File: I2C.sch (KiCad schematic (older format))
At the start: 13 parts

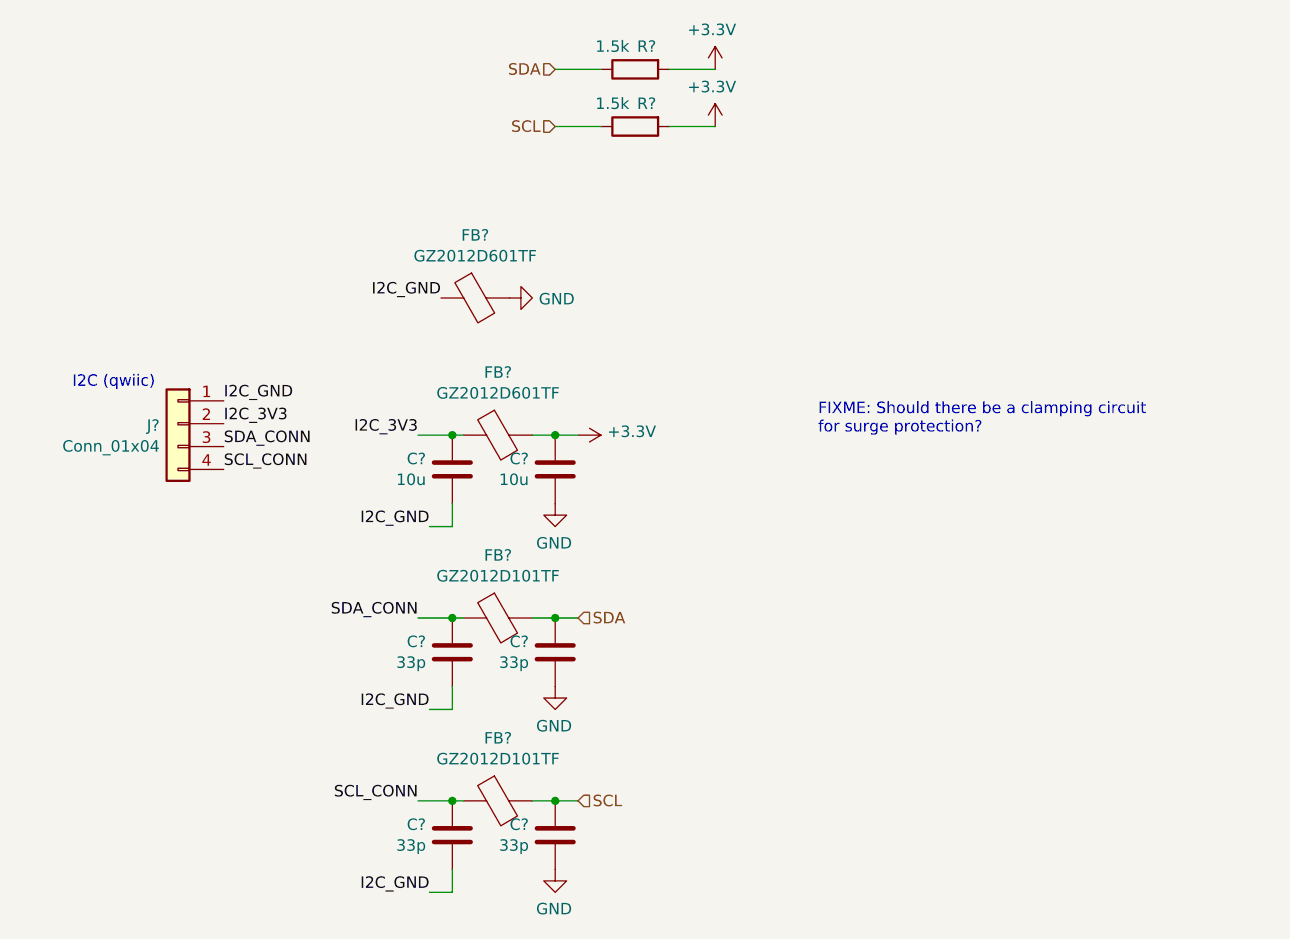
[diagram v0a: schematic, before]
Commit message: Update according to comments
Also add missing connectors and update the fuses
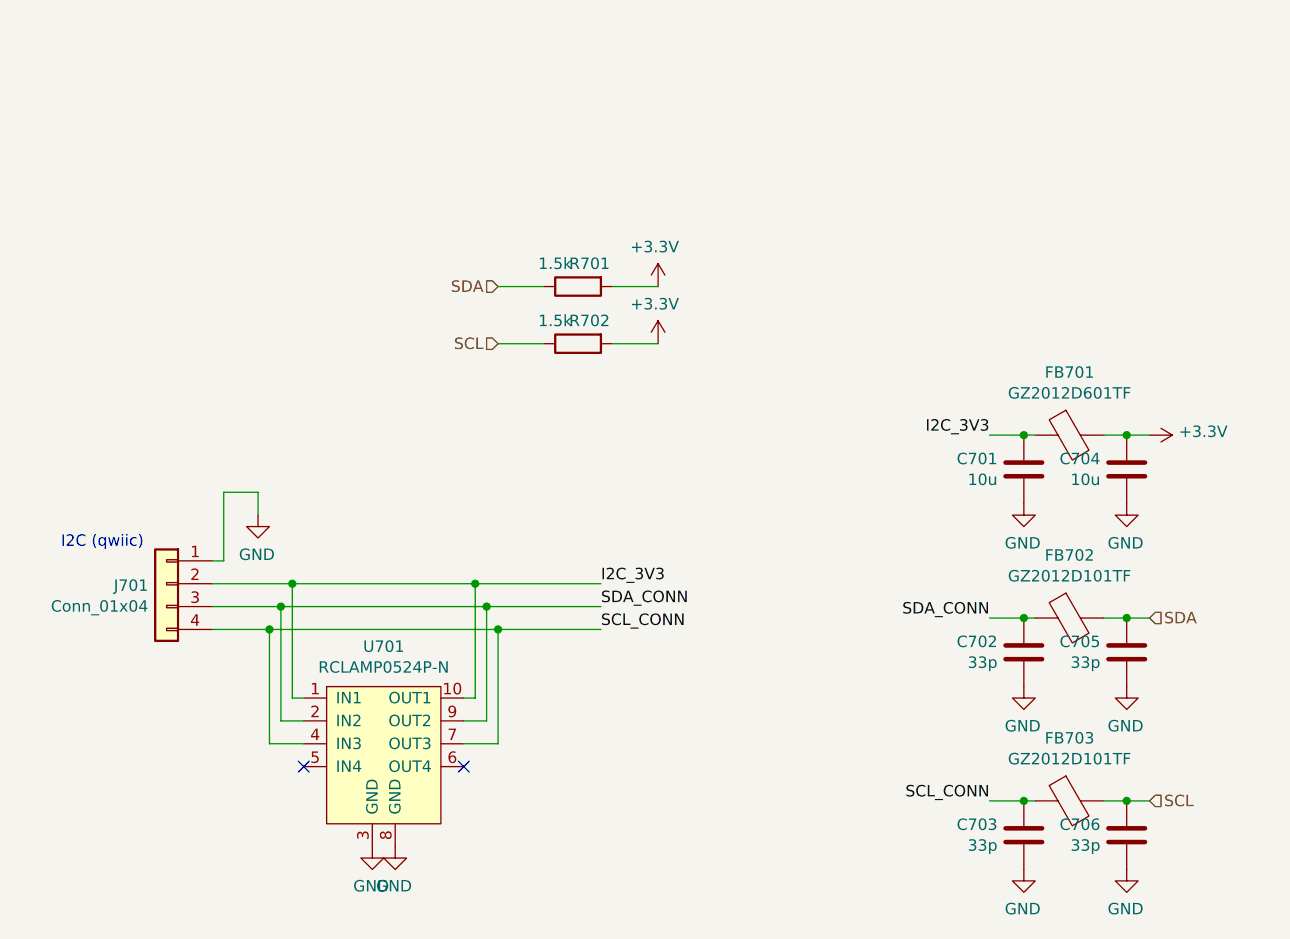
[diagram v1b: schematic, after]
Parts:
- removed FB?: GZ2012D601TF, symbol Device:Ferrite_Bead
- added U701: RCLAMP0524P-N, symbol SH-ESP32:RCLAMP0524P-N
- gave numbers to parts that had none: 12
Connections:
- net I2C_GND is gone; now on net GND: C701.2, C702.2, C703.2, J701.1 (Pin_1)
- net GND: now also U701.3 (GND), U701.8 (GND)
- net I2C_3V3: now also U701.1 (IN1), U701.10 (OUT1)
- net SCL_CONN: now also U701.4 (IN3), U701.7 (OUT3)
- net SDA_CONN: now also U701.2 (IN2), U701.9 (OUT2)
- no-connect marks 0 -> 2
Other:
- note removed: "FIXME: Should there be a clamping circuit\nfor surge protection?"
- moved on the sheet: C701, C702, C703, C704, C705, C706, FB701, FB702, FB703, J701, R701, R702

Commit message: Rough PCB layout
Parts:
- added J702: Conn_01x04, Connector_PinHeader_2.54mm:PinHeader_1x04_P2.54mm_Vertical, symbol Connector_Generic:Conn_01x04
- C701: value 10u -> 10uF; footprint (none) -> Capacitor_SMD:C_0402_1005Metric
- C702, C703: value 33p -> 33pF; footprint (none) -> Capacitor_SMD:C_0402_1005Metric
- C704: value 10u -> 10uF/50V; footprint (none) -> Capacitor_SMD:C_1206_3216Metric
- C705, C706: value 33p -> 33pF/50V; footprint (none) -> Capacitor_SMD:C_0603_1608Metric
- FB701, FB702, FB703: footprint (none) -> Inductor_SMD:L_0805_2012Metric
- J701: footprint (none) -> Connector_JST:JST_SH_BM04B-SRSS-TB_1x04-1MP_P1.00mm_Vertical
- R701, R702: footprint (none) -> Resistor_SMD:R_0402_1005Metric
- U701: footprint (none) -> Package_DFN_QFN:Diodes_UDFN-10_1.0x2.5mm_P0.5mm
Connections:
- net +3V3: now also C701.1; no longer C704.1
- net GND: now also J702.1 (Pin_1)
- net I2C_3V3: now also C704.1, J702.2 (Pin_2); no longer C701.1
- net SCL: now also C703.1; no longer C706.1
- net SCL_CONN: now also C706.1, J702.4 (Pin_4); no longer C703.1
- net SDA: now also C702.1; no longer C705.1
- net SDA_CONN: now also C705.1, J702.3 (Pin_3); no longer C702.1
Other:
- moved on the sheet: C701, C702, C703, C704, C705, C706

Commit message: Specified JLCPCB footprints for components
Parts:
- C701: LCSC (none) -> C15525
- C702, C703: LCSC (none) -> C1562
- C704: LCSC (none) -> C13585
- C705, C706: LCSC (none) -> C1663
- FB701: LCSC (none) -> C1017
- FB702, FB703: LCSC (none) -> C1015
- J701: LCSC (none) -> C145961
- J702: LCSC (none) -> C358686
- R701, R702: LCSC (none) -> C25867
- U701: LCSC (none) -> C316044
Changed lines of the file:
@@
 F 2 "Connector_JST:JST_SH_BM04B-SRSS-TB_1x04-1MP_P1.00mm_Vertical" H 1650 3350 50  0001 C CNN
 F 3 "~" H 1650 3350 50  0001 C CNN
+F 4 "C145961" H 1650 3350 50  0001 C CNN "LCSC"
 	1    1650 3350
 	-1   0    0    -1
@@
 F 2 "Capacitor_SMD:C_0603_1608Metric" H 5438 4300 50  0001 C CNN
 F 3 "~" H 5400 4450 50  0001 C CNN
+F 4 "C1663" H 5400 4450 50  0001 C CNN "LCSC"
 	1    5400 4450
 	-1   0    0    -1
@@
 F 2 "Capacitor_SMD:C_0603_1608Metric" H 5438 3500 50  0001 C CNN
 F 3 "~" H 5400 3650 50  0001 C CNN
+F 4 "C1663" H 5400 3650 50  0001 C CNN "LCSC"
 	1    5400 3650
 	-1   0    0    -1
@@
 F 2 "Capacitor_SMD:C_0402_1005Metric" H 5888 3500 50  0001 C CNN
 F 3 "~" H 5850 3650 50  0001 C CNN
+F 4 "C1562" H 5850 3650 50  0001 C CNN "LCSC"
 	1    5850 3650
 	1    0    0    -1
@@
 F 2 "Capacitor_SMD:C_0402_1005Metric" H 5888 4300 50  0001 C CNN
 F 3 "~" H 5850 4450 50  0001 C CNN
+F 4 "C1562" H 5850 4450 50  0001 C CNN "LCSC"
 	1    5850 4450
 	1    0    0    -1
@@
 F 2 "Capacitor_SMD:C_1206_3216Metric" H 5438 2700 50  0001 C CNN
 F 3 "~" H 5400 2850 50  0001 C CNN
+F 4 "C13585" H 5400 2850 50  0001 C CNN "LCSC"
 	1    5400 2850
 	-1   0    0    -1
@@
 F 2 "Capacitor_SMD:C_0402_1005Metric" H 5888 2700 50  0001 C CNN
 F 3 "~" H 5850 2850 50  0001 C CNN
+F 4 "C15525" H 5850 2850 50  0001 C CNN "LCSC"
 	1    5850 2850
 	1    0    0    -1
@@
 F 2 "Resistor_SMD:R_0402_1005Metric" V 3380 2050 50  0001 C CNN
 F 3 "~" H 3450 2050 50  0001 C CNN
+F 4 "C25867" H 3450 2050 50  0001 C CNN "LCSC"
 	1    3450 2050
 	0    -1   1    0
@@
 F 2 "Resistor_SMD:R_0402_1005Metric" V 3380 2300 50  0001 C CNN
 F 3 "~" H 3450 2300 50  0001 C CNN
+F 4 "C25867" H 3450 2300 50  0001 C CNN "LCSC"
 	1    3450 2300
 	0    -1   1    0
@@
 F 2 "Inductor_SMD:L_0805_2012Metric" V 5530 2700 50  0001 C CNN
 F 3 "~" H 5600 2700 50  0001 C CNN
+F 4 "C1017" H 5600 2700 50  0001 C CNN "LCSC"
 	1    5600 2700
 	0    -1   1    0
@@
 F 2 "Inductor_SMD:L_0805_2012Metric" V 5530 4300 50  0001 C CNN
 F 3 "~" H 5600 4300 50  0001 C CNN
+F 4 "C1015" H 5600 4300 50  0001 C CNN "LCSC"
 	1    5600 4300
 	0    -1   1    0
@@
 F 2 "Inductor_SMD:L_0805_2012Metric" V 5530 3500 50  0001 C CNN
 F 3 "~" H 5600 3500 50  0001 C CNN
+F 4 "C1015" H 5600 3500 50  0001 C CNN "LCSC"
 	1    5600 3500
 	0    -1   1    0
@@
 F 2 "Package_DFN_QFN:Diodes_UDFN-10_1.0x2.5mm_P0.5mm" H 2600 3950 50  0001 C CNN
 F 3 "" H 2600 3950 50  0001 C CNN
+F 4 "C316044" H 2600 4050 50  0001 C CNN "LCSC"
 	1    2600 4050
 	1    0    0    -1
@@
 F 2 "Connector_PinHeader_2.54mm:PinHeader_1x04_P2.54mm_Vertical" H 1650 2700 50  0001 C CNN
 F 3 "~" H 1650 2700 50  0001 C CNN
+F 4 "C358686" H 1650 2700 50  0001 C CNN "LCSC"
 	1    1650 2700
 	-1   0    0    -1

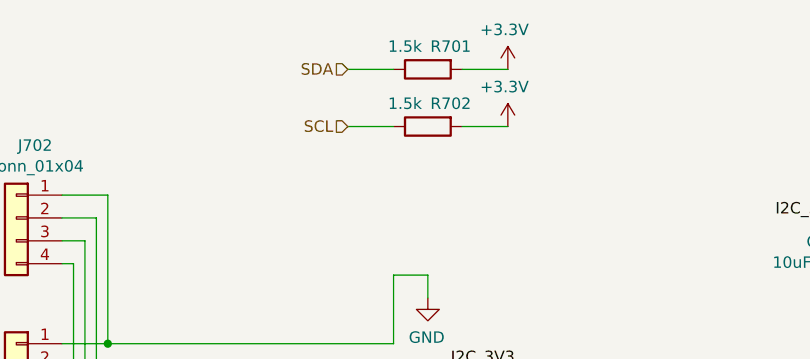
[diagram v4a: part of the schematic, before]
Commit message: Change I2C pullups to 2k due to missing JLCPCB basic parts(!)
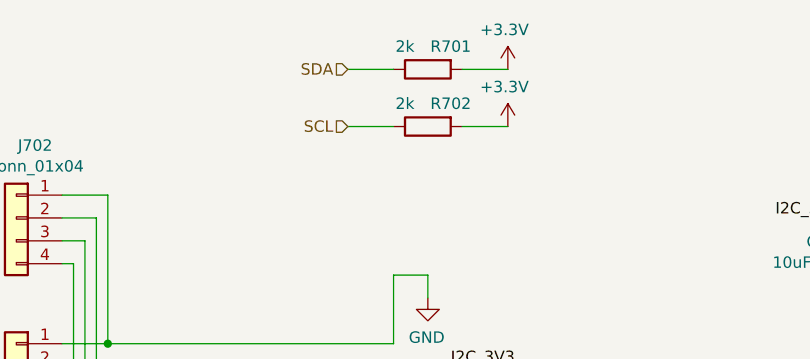
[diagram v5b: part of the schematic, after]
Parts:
- R701, R702: value 1.5k -> 2k; LCSC C25867 -> C4109
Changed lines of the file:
@@
 AR Path="/5F9BE197/5FA92D31" Ref="R701"  Part="1"
 F 0 "R701" V 3350 1950 50  0000 C CNN
-F 1 "1.5k" V 3350 2150 50  0000 C CNN
+F 1 "2k" V 3350 2150 50  0000 C CNN
 F 2 "Resistor_SMD:R_0402_1005Metric" V 3380 2050 50  0001 C CNN
 F 3 "~" H 3450 2050 50  0001 C CNN
-F 4 "C25867" H 3450 2050 50  0001 C CNN "LCSC"
+F 4 "C4109" H 3450 2050 50  0001 C CNN "LCSC"
 	1    3450 2050
 	0    -1   1    0
@@
 AR Path="/5F9BE197/5FA92D40" Ref="R702"  Part="1"
 F 0 "R702" V 3350 2200 50  0000 C CNN
-F 1 "1.5k" V 3350 2400 50  0000 C CNN
+F 1 "2k" V 3350 2400 50  0000 C CNN
 F 2 "Resistor_SMD:R_0402_1005Metric" V 3380 2300 50  0001 C CNN
 F 3 "~" H 3450 2300 50  0001 C CNN
-F 4 "C25867" H 3450 2300 50  0001 C CNN "LCSC"
+F 4 "C4109" H 3450 2300 50  0001 C CNN "LCSC"
 	1    3450 2300
 	0    -1   1    0

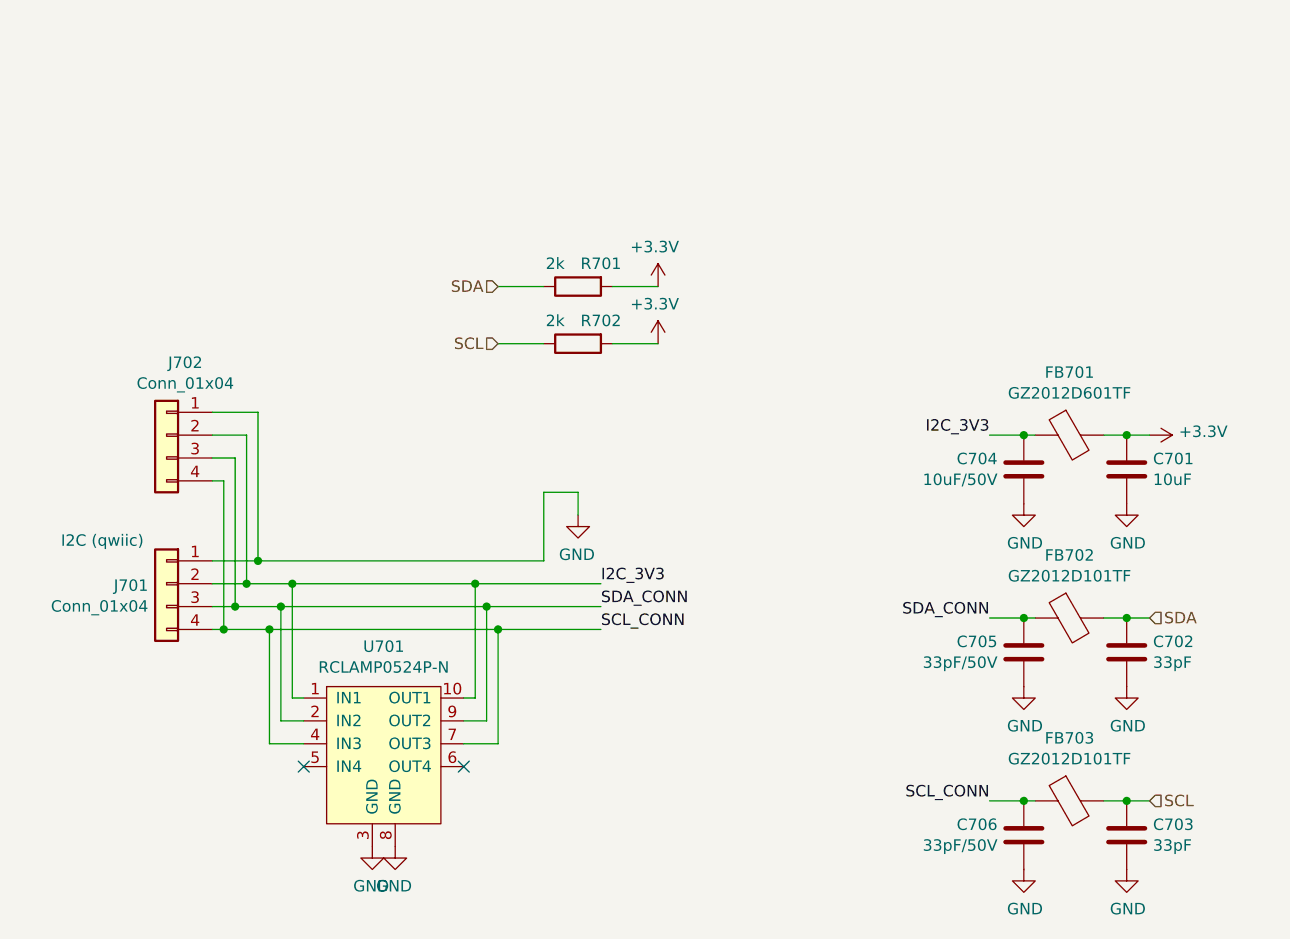
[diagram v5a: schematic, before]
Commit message: Support for OLED/LCD mini displays to direct plug to I2C header - Moved Pin header and Qwiic connectors and re-arranged I2C area. - Fixed silk screen accordingly - Also shoved USB conx 0.3mm and aligned tracks for matched USB tracks
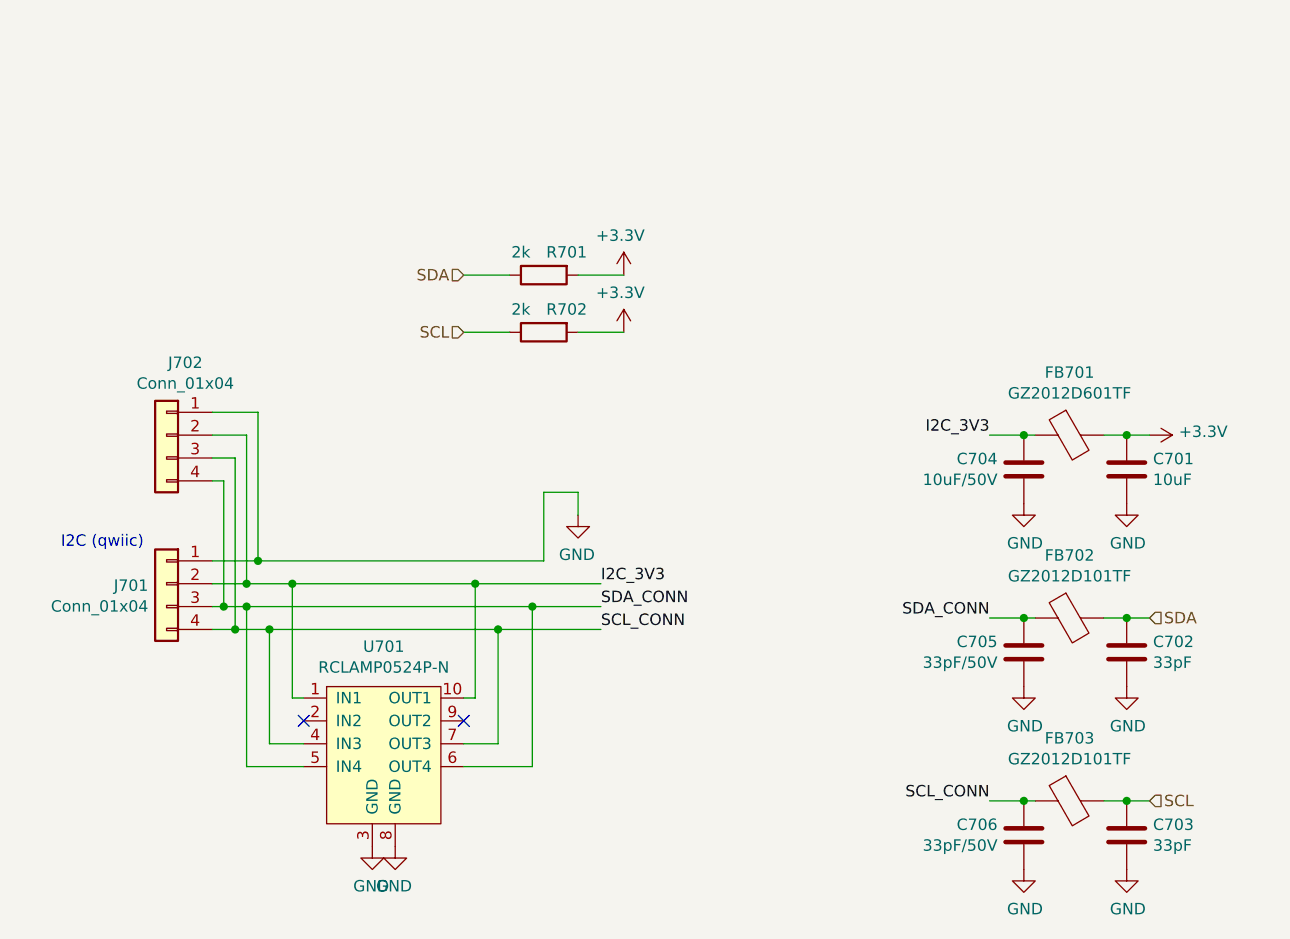
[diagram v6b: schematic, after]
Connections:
- net SCL_CONN: now also J702.3 (Pin_3); no longer J702.4 (Pin_4)
- net SDA_CONN: now also J702.4 (Pin_4), U701.5 (IN4), U701.6 (OUT4); no longer J702.3 (Pin_3), U701.2 (IN2), U701.9 (OUT2)
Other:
- moved on the sheet: R701, R702
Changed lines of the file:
@@
 L Device:R R?
 U 1 1 5FA92D31
-P 3450 2050
+P 3300 2000
 AR Path="/5F89C30A/5FA92D31" Ref="R?"  Part="1"
 AR Path="/5FA92D31" Ref="R?"  Part="1"
 AR Path="/5F9BE197/5FA92D31" Ref="R701"  Part="1"
-F 0 "R701" V 3350 1950 50  0000 C CNN
-F 1 "2k" V 3350 2150 50  0000 C CNN
-F 2 "Resistor_SMD:R_0402_1005Metric" V 3380 2050 50  0001 C CNN
-F 3 "~" H 3450 2050 50  0001 C CNN
-F 4 "C4109" H 3450 2050 50  0001 C CNN "LCSC"
-	1    3450 2050
-	0    -1   1    0
-$EndComp
-Wire Wire Line
-	3800 2050 3600 2050
-Wire Wire Line
-	3100 2050 3300 2050
+F 0 "R701" V 3200 1900 50  0000 C CNN
+F 1 "2k" V 3200 2100 50  0000 C CNN
+F 2 "Resistor_SMD:R_0402_1005Metric" V 3230 2000 50  0001 C CNN
+F 3 "~" H 3300 2000 50  0001 C CNN
+F 4 "C4109" H 3300 2000 50  0001 C CNN "LCSC"
+	1    3300 2000
+	0    -1   1    0
+$EndComp
+Wire Wire Line
+	3650 2000 3450 2000
+Wire Wire Line
+	2950 2000 3150 2000
 $Comp
 L power:+3.3V #PWR?
 U 1 1 5FA92D3A
-P 3800 2050
+P 3650 2000
 AR Path="/5FA92D3A" Ref="#PWR?"  Part="1"
 AR Path="/5F9BE197/5FA92D3A" Ref="#PWR0704"  Part="1"
-F 0 "#PWR0704" H 3800 1900 50  0001 C CNN
-F 1 "+3.3V" H 3815 2223 50  0000 C CNN
-F 2 "" H 3800 2050 50  0001 C CNN
-F 3 "" H 3800 2050 50  0001 C CNN
-	1    3800 2050
+F 0 "#PWR0704" H 3650 1850 50  0001 C CNN
+F 1 "+3.3V" H 3665 2173 50  0000 C CNN
+F 2 "" H 3650 2000 50  0001 C CNN
+F 3 "" H 3650 2000 50  0001 C CNN
+	1    3650 2000
 	-1   0    0    -1
 $EndComp
@@
 L Device:R R?
 U 1 1 5FA92D40
-P 3450 2300
+P 3300 2250
 AR Path="/5F89C30A/5FA92D40" Ref="R?"  Part="1"
 AR Path="/5FA92D40" Ref="R?"  Part="1"
 AR Path="/5F9BE197/5FA92D40" Ref="R702"  Part="1"
-F 0 "R702" V 3350 2200 50  0000 C CNN
-F 1 "2k" V 3350 2400 50  0000 C CNN
-F 2 "Resistor_SMD:R_0402_1005Metric" V 3380 2300 50  0001 C CNN
-F 3 "~" H 3450 2300 50  0001 C CNN
-F 4 "C4109" H 3450 2300 50  0001 C CNN "LCSC"
-	1    3450 2300
-	0    -1   1    0
-$EndComp
-Wire Wire Line
-	3800 2300 3600 2300
-Wire Wire Line
-	3100 2300 3300 2300
+F 0 "R702" V 3200 2150 50  0000 C CNN
+F 1 "2k" V 3200 2350 50  0000 C CNN
+F 2 "Resistor_SMD:R_0402_1005Metric" V 3230 2250 50  0001 C CNN
+F 3 "~" H 3300 2250 50  0001 C CNN
+F 4 "C4109" H 3300 2250 50  0001 C CNN "LCSC"
+	1    3300 2250
+	0    -1   1    0
+$EndComp
+Wire Wire Line
+	3650 2250 3450 2250
+Wire Wire Line
+	2950 2250 3150 2250
 $Comp
 L power:+3.3V #PWR?
 U 1 1 5FA92D49
-P 3800 2300
+P 3650 2250
 AR Path="/5FA92D49" Ref="#PWR?"  Part="1"
 AR Path="/5F9BE197/5FA92D49" Ref="#PWR0705"  Part="1"
-F 0 "#PWR0705" H 3800 2150 50  0001 C CNN
-F 1 "+3.3V" H 3815 2473 50  0000 C CNN
-F 2 "" H 3800 2300 50  0001 C CNN
-F 3 "" H 3800 2300 50  0001 C CNN
-	1    3800 2300
+F 0 "#PWR0705" H 3650 2100 50  0001 C CNN
+F 1 "+3.3V" H 3665 2423 50  0000 C CNN
+F 2 "" H 3650 2250 50  0001 C CNN
+F 3 "" H 3650 2250 50  0001 C CNN
+	1    3650 2250
 	-1   0    0    -1
 $EndComp
@@
 	0    -1   1    0
 $EndComp
-Text HLabel 3100 2050 0    50   Input ~ 0
+Text HLabel 2950 2000 0    50   Input ~ 0
 SDA
-Text HLabel 3100 2300 0    50   Input ~ 0
+Text HLabel 2950 2250 0    50   Input ~ 0
 SCL
 Text HLabel 5950 3500 2    50   Input ~ 0
@@
 	3550 3350 3000 3350
 Wire Wire Line
-	1850 3450 1950 3450
-Wire Wire Line
 	3550 3550 3100 3550
 Wire Wire Line
@@
 	2200 3350 2000 3350
 Wire Wire Line
-	2150 3450 2150 3950
-Wire Wire Line
-	2150 3950 2250 3950
-Connection ~ 2150 3450
-Wire Wire Line
-	2150 3450 3050 3450
-Wire Wire Line
-	2950 3950 3050 3950
-Wire Wire Line
-	3050 3950 3050 3450
-Connection ~ 3050 3450
-Wire Wire Line
-	3050 3450 3550 3450
-Wire Wire Line
 	3100 3550 3100 4050
 Wire Wire Line
@@
 	2100 4050 2100 3550
 Connection ~ 2100 3550
-Wire Wire Line
-	2100 3550 1900 3550
-NoConn ~ 2250 4150
-NoConn ~ 2950 4150
+NoConn ~ 2250 3950
+NoConn ~ 2950 3950
 $Comp
 L power:GND #PWR?
@@
 $EndComp
 Wire Wire Line
-	1850 2900 1900 2900
-Wire Wire Line
-	1900 2900 1900 3550
-Connection ~ 1900 3550
-Wire Wire Line
-	1900 3550 1850 3550
-Wire Wire Line
-	1850 2800 1950 2800
-Wire Wire Line
-	1950 2800 1950 3450
-Connection ~ 1950 3450
-Wire Wire Line
-	1950 3450 2150 3450
-Wire Wire Line
 	1850 2700 2000 2700
 Wire Wire Line
@@
 Wire Wire Line
 	5850 4300 5950 4300
+Wire Wire Line
+	1850 3450 1900 3450
+Wire Wire Line
+	1850 3550 1950 3550
+Wire Wire Line
+	1850 2800 1950 2800
+Wire Wire Line
+	1950 2800 1950 3550
+Connection ~ 1950 3550
+Wire Wire Line
+	1950 3550 2100 3550
+Wire Wire Line
+	1850 2900 1900 2900
+Wire Wire Line
+	1900 2900 1900 3450
+Connection ~ 1900 3450
+Wire Wire Line
+	1900 3450 2000 3450
+Wire Wire Line
+	2000 4150 2000 3450
+Connection ~ 2000 3450
+Wire Wire Line
+	2000 3450 3250 3450
+Wire Wire Line
+	2950 4150 3250 4150
+Wire Wire Line
+	3250 4150 3250 3450
+Connection ~ 3250 3450
+Wire Wire Line
+	3250 3450 3550 3450
+Wire Wire Line
+	2000 4150 2250 4150
 $EndSCHEMATC
